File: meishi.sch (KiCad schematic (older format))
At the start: 31 parts, among them J1 USB_B_Micro, J2 Conn_01x05, SW1 SW_Push, SW11 PG1350_Socket, SW12 PG1350_Socket, SW13 PG1350_Socket, SW14 PG1350_Socket, SW15 PG1350_Socket, SW2 SW_DIP_x01, SW21 PG1350_Socket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

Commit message: fix component layout
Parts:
- added R1001: 10k, Resistor_SMD:R_0603_1608Metric, symbol Device:R_Small
- C1: value C_Small -> 100n
- R1: value R_Small -> 100k
- SW2: footprint Button_Switch_SMD:SW_DIP_SPSTx01_Slide_6.7x4.1mm_W6.73mm_P2.54mm_LowProfile_JPin -> Button_Switch_SMD:SW_DIP_SPSTx01_Slide_Copal_CHS-01B_W7.62mm_P1.27mm
- U3: symbol random-keyboard-parts:PRTR5V0U2X -> meishi-rescue:PRTR5V0U2X-random-keyboard-parts
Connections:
- net NRST: now also R1001.2
- net VDD: now also R1001.1
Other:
- moved on the sheet: C1, SW1
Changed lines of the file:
@@
 L Device:C_Small C1
 U 1 1 5C6F4FE2
-P 1300 6300
-F 0 "C1" H 1392 6346 50  0000 L CNN
-F 1 "C_Small" H 1392 6255 50  0000 L CNN
-F 2 "Capacitor_SMD:C_0603_1608Metric" H 1300 6300 50  0001 C CNN
-F 3 "~" H 1300 6300 50  0001 C CNN
-	1    1300 6300
+P 1275 6725
+F 0 "C1" H 1367 6771 50  0000 L CNN
+F 1 "100n" H 1367 6680 50  0000 L CNN
+F 2 "Capacitor_SMD:C_0603_1608Metric" H 1275 6725 50  0001 C CNN
+F 3 "~" H 1275 6725 50  0001 C CNN
+	1    1275 6725
 	1    0    0    -1
 $EndComp
@@
 L Switch:SW_Push SW1
 U 1 1 5C6F5096
-P 1650 6300
-F 0 "SW1" V 1604 6448 50  0000 L CNN
-F 1 "SW_Push" V 1695 6448 50  0000 L CNN
-F 2 "Button_Switch_SMD:SW_SPST_CK_RS282G05A3" H 1650 6500 50  0001 C CNN
-F 3 "" H 1650 6500 50  0001 C CNN
-	1    1650 6300
+P 1625 6725
+F 0 "SW1" V 1579 6873 50  0000 L CNN
+F 1 "SW_Push" V 1670 6873 50  0000 L CNN
+F 2 "Button_Switch_SMD:SW_SPST_CK_RS282G05A3" H 1625 6925 50  0001 C CNN
+F 3 "" H 1625 6925 50  0001 C CNN
+	1    1625 6725
 	0    1    1    0
 $EndComp
@@
 L power:GND #PWR0113
 U 1 1 5C6F5132
-P 1650 6600
-F 0 "#PWR0113" H 1650 6350 50  0001 C CNN
-F 1 "GND" H 1655 6427 50  0000 C CNN
-F 2 "" H 1650 6600 50  0001 C CNN
-F 3 "" H 1650 6600 50  0001 C CNN
-	1    1650 6600
-	1    0    0    -1
-$EndComp
-Wire Wire Line
-	1650 6500 1650 6550
-Wire Wire Line
-	1300 6400 1300 6550
-Wire Wire Line
-	1300 6550 1650 6550
-Connection ~ 1650 6550
-Wire Wire Line
-	1650 6550 1650 6600
-Text GLabel 1050 6000 0    50   Input ~ 0
+P 1625 7025
+F 0 "#PWR0113" H 1625 6775 50  0001 C CNN
+F 1 "GND" H 1630 6852 50  0000 C CNN
+F 2 "" H 1625 7025 50  0001 C CNN
+F 3 "" H 1625 7025 50  0001 C CNN
+	1    1625 7025
+	1    0    0    -1
+$EndComp
+Wire Wire Line
+	1625 6925 1625 6975
+Wire Wire Line
+	1275 6825 1275 6975
+Wire Wire Line
+	1275 6975 1625 6975
+Connection ~ 1625 6975
+Wire Wire Line
+	1625 6975 1625 7025
+Text GLabel 1025 6425 0    50   Input ~ 0
 NRST
 Wire Wire Line
-	1050 6000 1300 6000
-Wire Wire Line
-	1650 6000 1650 6100
-Wire Wire Line
-	1300 6200 1300 6000
-Connection ~ 1300 6000
-Wire Wire Line
-	1300 6000 1650 6000
+	1025 6425 1275 6425
+Wire Wire Line
+	1625 6425 1625 6525
+Wire Wire Line
+	1275 6625 1275 6425
+Connection ~ 1275 6425
+Wire Wire Line
+	1275 6425 1625 6425
 Text GLabel 1150 2750 0    50   Input ~ 0
 BOOT0
@@
 	2250 1550 2200 1550
 $Comp
-L random-keyboard-parts:PRTR5V0U2X U3
+L meishi-rescue:PRTR5V0U2X-random-keyboard-parts U3
 U 1 1 5C6FEFAD
 P 2300 5200
@@
 F 0 "SW2" H 5400 6767 50  0000 C CNN
 F 1 "SW_DIP_x01" H 5400 6676 50  0000 C CNN
-F 2 "Button_Switch_SMD:SW_DIP_SPSTx01_Slide_6.7x4.1mm_W6.73mm_P2.54mm_LowProfile_JPin" H 5400 6500 50  0001 C CNN
+F 2 "Button_Switch_SMD:SW_DIP_SPSTx01_Slide_Copal_CHS-01B_W7.62mm_P1.27mm" H 5400 6500 50  0001 C CNN
 F 3 "" H 5400 6500 50  0001 C CNN
 	1    5400 6500
@@
 P 5050 6650
 F 0 "R1" H 5109 6696 50  0000 L CNN
-F 1 "R_Small" H 5109 6605 50  0000 L CNN
+F 1 "100k" H 5109 6605 50  0000 L CNN
 F 2 "Resistor_SMD:R_0603_1608Metric" H 5050 6650 50  0001 C CNN
 F 3 "~" H 5050 6650 50  0001 C CNN
@@
 Wire Wire Line
 	5750 6500 5750 6250
+$Comp
+L power:VDD #PWR0121
+U 1 1 5C6BD820
+P 1975 6250
+F 0 "#PWR0121" H 1975 6100 50  0001 C CNN
+F 1 "VDD" H 1992 6423 50  0000 C CNN
+F 2 "" H 1975 6250 50  0001 C CNN
+F 3 "" H 1975 6250 50  0001 C CNN
+	1    1975 6250
+	1    0    0    -1
+$EndComp
+Wire Wire Line
+	1975 6425 1975 6250
+$Comp
+L Device:R_Small R1001
+U 1 1 5C6D0E87
+P 1800 6425
+F 0 "R1001" V 1604 6425 50  0000 C CNN
+F 1 "10k" V 1695 6425 50  0000 C CNN
+F 2 "Resistor_SMD:R_0603_1608Metric" H 1800 6425 50  0001 C CNN
+F 3 "~" H 1800 6425 50  0001 C CNN
+	1    1800 6425
+	0    1    1    0
+$EndComp
+Wire Wire Line
+	1625 6425 1700 6425
+Connection ~ 1625 6425
+Wire Wire Line
+	1900 6425 1975 6425
 $EndSCHEMATC

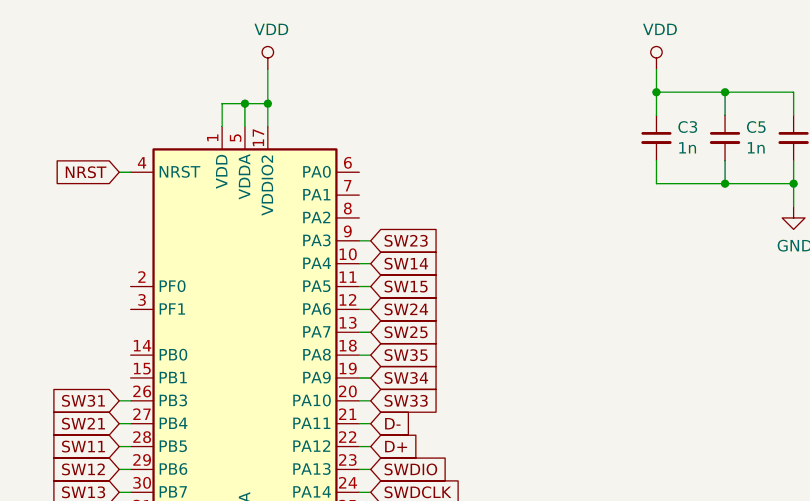
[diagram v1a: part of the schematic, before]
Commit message: fix unconnected SW22 to PA2 silk layer fix
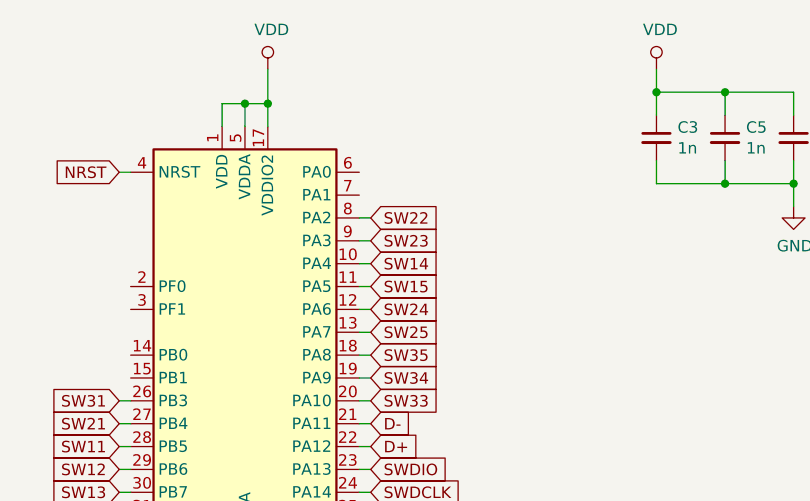
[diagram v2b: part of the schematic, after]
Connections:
- net SW22: now also U1.8 (PA2)
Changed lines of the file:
@@
 Wire Wire Line
 	1900 6425 1975 6425
+Text GLabel 2250 1450 2    50   Input ~ 0
+SW22
+Wire Wire Line
+	2250 1450 2200 1450
 $EndSCHEMATC

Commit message: make changes
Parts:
- removed J1: USB_B_Micro, Connector_USB:USB_Micro-B_Molex-105017-0001, symbol Connector:USB_B_Micro
- added J1001: E8124-015-01, random-keyboard-parts:SparkFun_15111, symbol Connector:USB_C_Receptacle_USB2.0
- added J3: Conn_01x04, Connector_JST:JST_SH_SM04B-SRSS-TB_1x04-1MP_P1.00mm_Horizontal, symbol Connector_Generic:Conn_01x04
- added R1001, R1002: 5.1k, DigiKey:0603, symbol Device:R_Small
- added R2: R_Small, DigiKey:0603, symbol Device:R_Small
- added R3: R_Small, Resistor_SMD:R_0603_1608Metric, symbol Device:R_Small
- added R4: 39k, Resistor_SMD:R_0603_1608Metric, symbol Device:R_Small
- added R5: 68k, Resistor_SMD:R_0603_1608Metric, symbol Device:R_Small
- C1, C2, C4: footprint Capacitor_SMD:C_0603_1608Metric -> DigiKey:0603
- C3, C5, C6: value 1n -> 100n; footprint Capacitor_SMD:C_0603_1608Metric -> DigiKey:0603
- R1: footprint Resistor_SMD:R_0603_1608Metric -> DigiKey:0603
- R6: renamed from R1001; footprint Resistor_SMD:R_0603_1608Metric -> DigiKey:0603
- U1: value STM32F042K4Tx -> STM32F042K6U6; footprint Package_QFP:LQFP-32_7x7mm_P0.8mm -> DigiKey:QFN-32-1EP_5x5mm; symbol MCU_ST_STM32F0:STM32F042K4Tx -> MCU_ST_STM32F0:STM32F042K6Ux
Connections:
- net BOOT0: now also U1.32 (PB8); no longer U1.31 (PB8)
- net D+: now also J1001.A6 (D+), J1001.B6 (D+)
- net D-: now also J1001.A7 (D-), J1001.B7 (D-)
- net GND: now also U1.33 (VSS), J1001.A1 (GND), J1001.A12 (GND), J1001.B1 (GND), J1001.B12 (GND), J1001.S1 (SHIELD), J3.4 (Pin_4), R1001.2, R1002.1, R5.2; no longer U1.16 (VSS), U1.32 (VSSA)
- net VBUS: now also F1.2, J1001.A4 (VBUS), J1001.A9 (VBUS), J1001.B4 (VBUS), J1001.B9 (VBUS), R4.1
- net VDD: now also J3.2 (Pin_2), R2.2, R3.1
- net VBUS_Sense: now reaches U1.15 (PB1)
- net VBUS_Sense: now also R4.2, R5.1
- net I2C1_SDA: now reaches U1.2 (PF0)
- net I2C1_SDA: now also J3.1 (Pin_1), R2.1
- net I2C1_SCL: now reaches U1.3 (PF1)
- net I2C1_SCL: now also J3.3 (Pin_3), R3.2
- new net: J1001.A5 (CC1), R1002.2
- new net: J1001.B5 (CC2), R1001.1
- no-connect marks 1 -> 2
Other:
- moved on the sheet: C2, C4, D2, F1, U2, U3
